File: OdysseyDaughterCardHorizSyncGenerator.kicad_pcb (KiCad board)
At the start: 2 copper layers, 47.8 x 46.6 mm, 16 parts, among them Q1 BC547B, Q2 BC556B, Q3 2N3904, X1 OdysseyDaughterCard

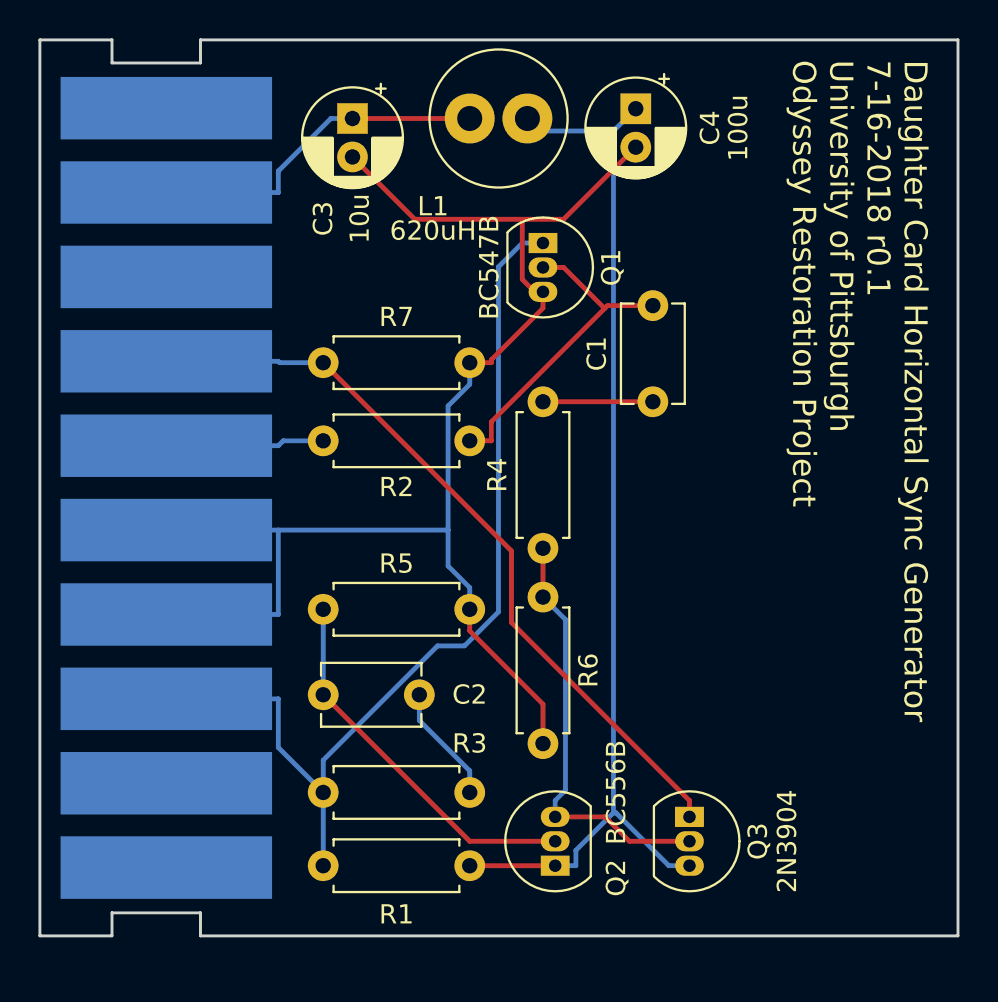
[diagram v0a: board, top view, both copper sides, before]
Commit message: V0.3 fixes backwards transistor in schematic, regenerated gerbers
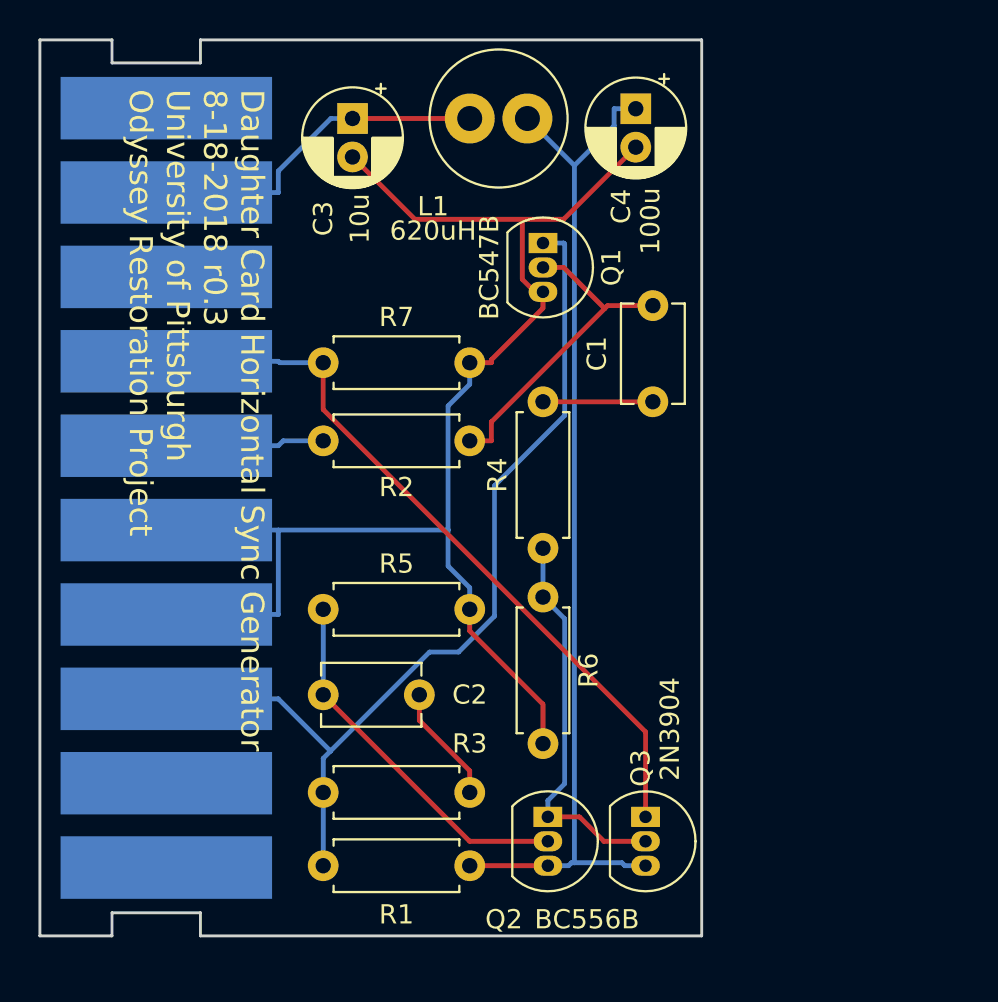
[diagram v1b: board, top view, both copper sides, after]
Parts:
- moved Q2 2.57 mm to (148.8, 118.1), turned to 270 degrees
- moved Q3 2.29 mm to (153.9, 118.1)
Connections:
- Q2 pad 1: Net-(C4-Pad1) -> Net-(Q2-Pad1)
- Q2 pad 3: Net-(Q2-Pad3) -> Net-(C4-Pad1)
- Q3 pad 2: Net-(Q2-Pad3) -> Net-(Q2-Pad1)
- R4 pad 1: Net-(Q2-Pad3) -> Net-(Q2-Pad1)
- R6 pad 1: Net-(Q2-Pad3) -> Net-(Q2-Pad1)
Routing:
- net Net-(Q2-Pad3): track 22.2 -> 0.00 mm
- net Net-(Q2-Pad1): track 0.00 -> 20.4 mm
- net Net-(C4-Pad1): track 56.0 -> 53.9 mm
- net /Card3: track 50.2 -> 49.2 mm
- net /Card7: track 39.7 -> 38.8 mm
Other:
- board size 47.8 x 46.6 mm -> 34.4 x 46.6 mm
- board text added: "Daughter Card Horizontal Sync Generator 8-18-2018 r0.3 University of Pittsburgh Odyssey Restoration Project"
- board text removed: "Daughter Card Horizontal Sync Generator 7-16-2018 r0.1 University of Pittsburgh Odyssey Restoration Project"
